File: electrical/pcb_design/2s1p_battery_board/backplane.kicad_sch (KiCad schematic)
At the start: 21 parts, among them J10 TE_Connectivity_7-5530843-7, J11 TE_Connectivity_7-5530843-7, J12 TE_Connectivity_7-5530843-7, J13 TE_Connectivity_7-5530843-7, J14 TE_Connectivity_7-5530843-7, J15 TE_Connectivity_7-5530843-7, J16 TE_Connectivity_7-5530843-7, J9 TE_Connectivity_7-5530843-7, U3 TCAN330

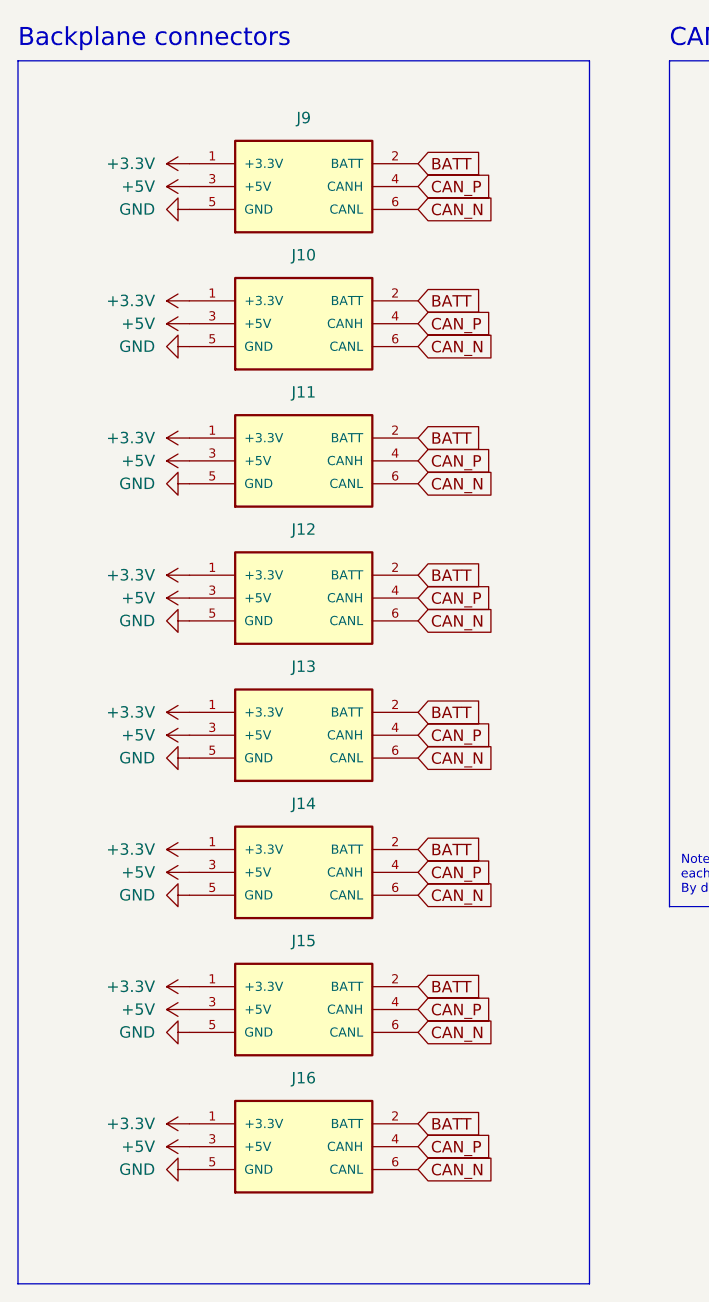
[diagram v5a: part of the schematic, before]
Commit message: Marked several parts as DNP; we will assemble those parts by hand. Generated production files. Regenerated 3D model.
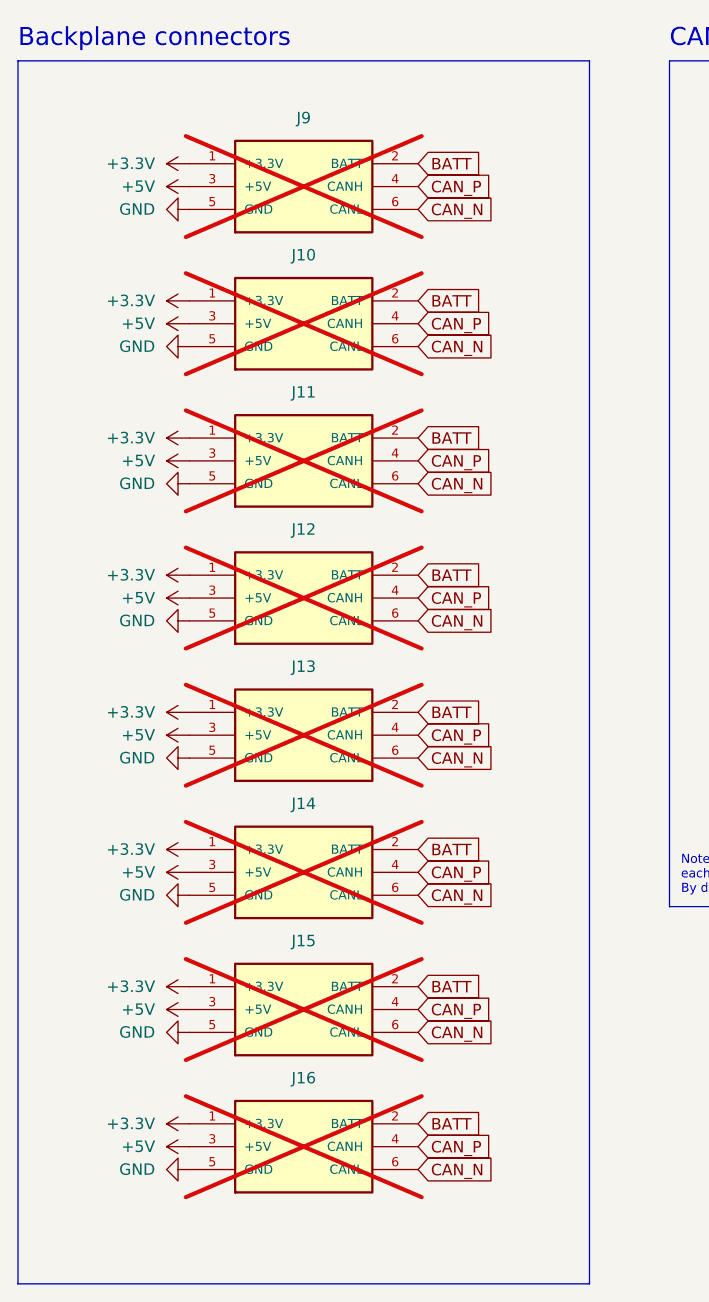
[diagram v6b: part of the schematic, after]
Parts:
- J10, J11, J12, J13, J14, J15, J16, J9: now not fitted
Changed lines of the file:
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@@
   )
   (symbol (lib_id "TVSC:Backplane_Connector_Consumer") (at 101.6 93.98 0) (unit 1)
-    (in_bom yes) (on_board yes) (dnp no) (fields_autoplaced)
+    (in_bom yes) (on_board yes) (dnp yes) (fields_autoplaced)
     (property "Reference" "J12" (at 101.6 86.36 0)
       (effects (font (size 1.27 1.27)))
@@
   )
   (symbol (lib_id "TVSC:Backplane_Connector_Consumer") (at 101.6 109.22 0) (unit 1)
-    (in_bom yes) (on_board yes) (dnp no) (fields_autoplaced)
+    (in_bom yes) (on_board yes) (dnp yes) (fields_autoplaced)
     (property "Reference" "J13" (at 101.6 101.6 0)
       (effects (font (size 1.27 1.27)))
@@
   )
   (symbol (lib_id "TVSC:Backplane_Connector_Consumer") (at 101.6 124.46 0) (unit 1)
-    (in_bom yes) (on_board yes) (dnp no) (fields_autoplaced)
+    (in_bom yes) (on_board yes) (dnp yes) (fields_autoplaced)
     (property "Reference" "J14" (at 101.6 116.84 0)
       (effects (font (size 1.27 1.27)))
@@
   )
   (symbol (lib_id "TVSC:Backplane_Connector_Consumer") (at 101.6 154.94 0) (unit 1)
-    (in_bom yes) (on_board yes) (dnp no) (fields_autoplaced)
+    (in_bom yes) (on_board yes) (dnp yes) (fields_autoplaced)
     (property "Reference" "J16" (at 101.6 147.32 0)
       (effects (font (size 1.27 1.27)))
@@
   )
   (symbol (lib_id "TVSC:Backplane_Connector_Consumer") (at 101.6 78.74 0) (unit 1)
-    (in_bom yes) (on_board yes) (dnp no) (fields_autoplaced)
+    (in_bom yes) (on_board yes) (dnp yes) (fields_autoplaced)
     (property "Reference" "J11" (at 101.6 71.12 0)
       (effects (font (size 1.27 1.27)))
@@
   )
   (symbol (lib_id "TVSC:Backplane_Connector_Consumer") (at 101.6 63.5 0) (unit 1)
-    (in_bom yes) (on_board yes) (dnp no) (fields_autoplaced)
+    (in_bom yes) (on_board yes) (dnp yes) (fields_autoplaced)
     (property "Reference" "J10" (at 101.6 55.88 0)
       (effects (font (size 1.27 1.27)))
@@
   )
   (symbol (lib_id "TVSC:Backplane_Connector_Consumer") (at 101.6 48.26 0) (unit 1)
-    (in_bom yes) (on_board yes) (dnp no) (fields_autoplaced)
+    (in_bom yes) (on_board yes) (dnp yes) (fields_autoplaced)
     (property "Reference" "J9" (at 101.6 40.64 0)
       (effects (font (size 1.27 1.27)))
@@
   )
   (symbol (lib_id "TVSC:Backplane_Connector_Consumer") (at 101.6 139.7 0) (unit 1)
-    (in_bom yes) (on_board yes) (dnp no) (fields_autoplaced)
+    (in_bom yes) (on_board yes) (dnp yes) (fields_autoplaced)
     (property "Reference" "J15" (at 101.6 132.08 0)
       (effects (font (size 1.27 1.27)))

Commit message: Checkpointing work rearranging backplane pin-out
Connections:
- net +5V is gone; now on net GND: J10.3 (GND), J11.3 (GND), J12.3 (GND), J13.3 (GND), J14.3 (GND), J15.3 (GND), J16.3 (GND), J9.3 (GND)
- net CAN_P: now also J10.5 (CANH), J11.5 (CANH), J12.5 (CANH), J13.5 (CANH), J14.5 (CANH), J15.5 (CANH), J16.5 (CANH), J9.5 (CANH); no longer J10.4 (CANH), J11.4 (CANH), J12.4 (CANH), J13.4 (CANH), J14.4 (CANH), J15.4 (CANH), J16.4 (CANH), J9.4 (CANH)
- net GND: no longer J10.5 (GND), J11.5 (GND), J12.5 (GND), J13.5 (GND), J14.5 (GND), J15.5 (GND), J16.5 (GND), J9.5 (GND)
- no-connect marks 2 -> 10
